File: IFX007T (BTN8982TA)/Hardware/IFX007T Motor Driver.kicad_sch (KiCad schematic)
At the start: 16 parts, among them M1 12V, SW1 ENABLE, SW2 HSS, SW3 HSS, U1 IFX007T, U2 IFX007T

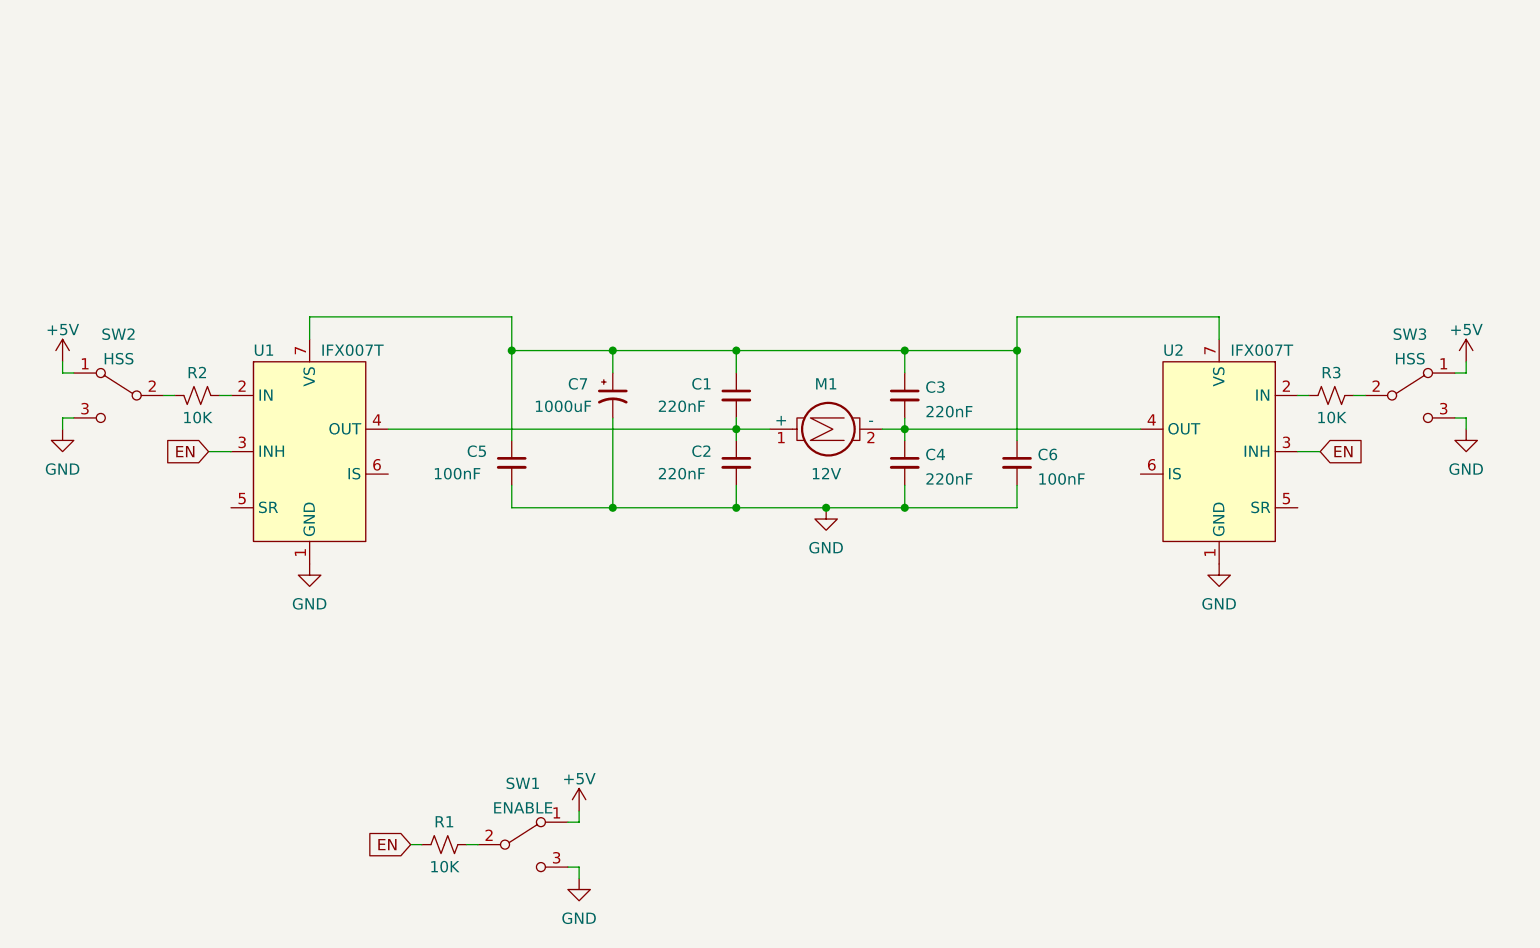
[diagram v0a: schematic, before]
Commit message: Add IS and SR circuitry
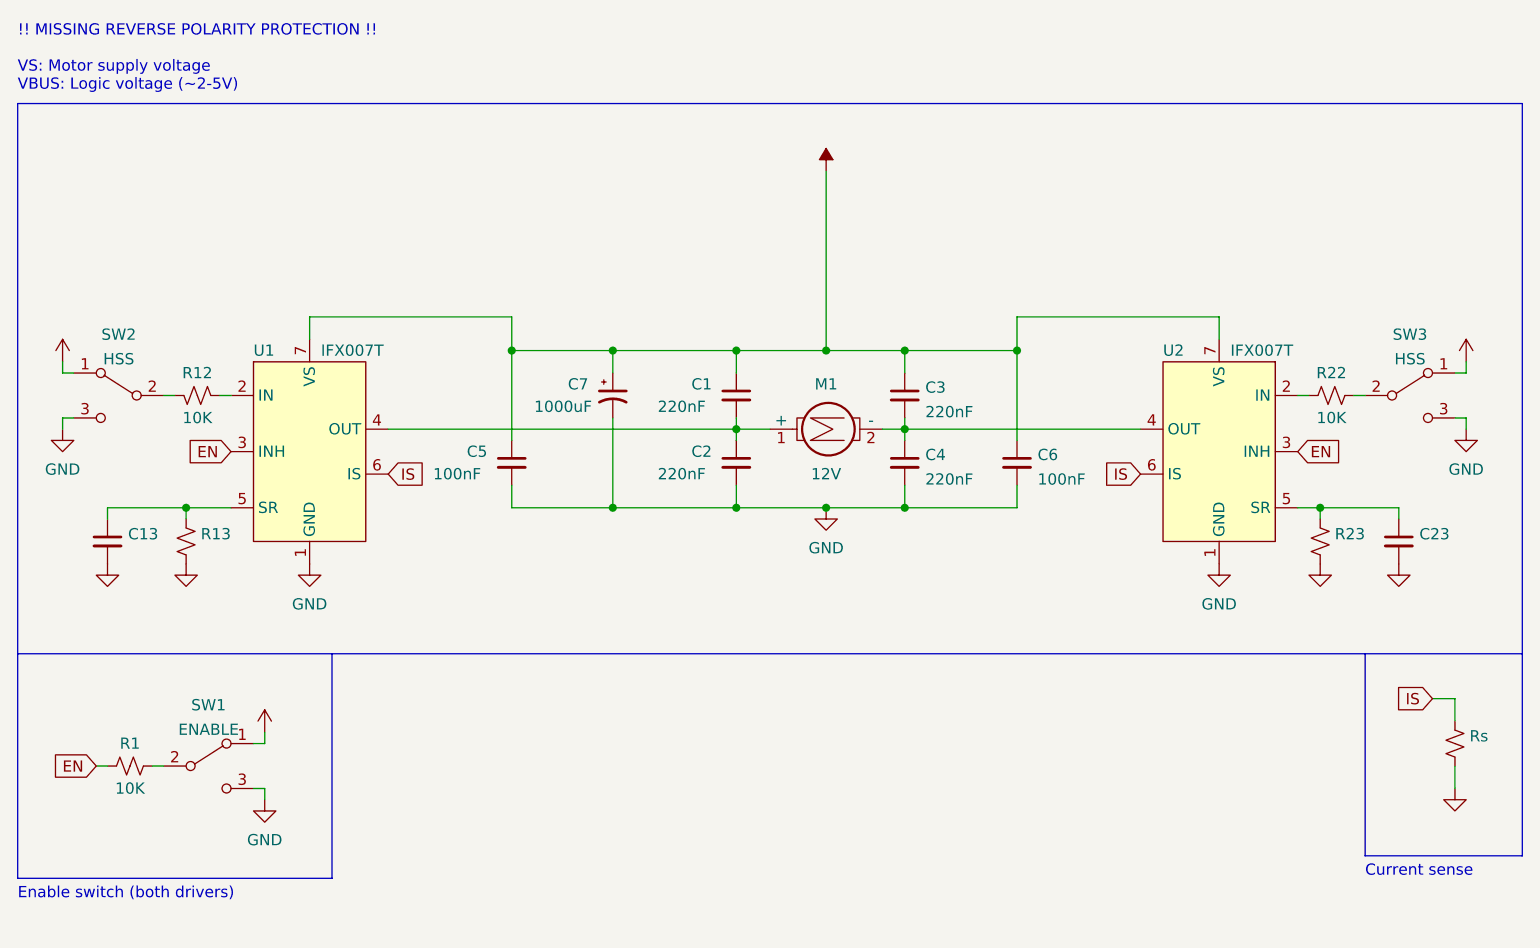
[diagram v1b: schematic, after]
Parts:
- added C13, C23: (no value), symbol Device:C_Small
- added R13, R23, Rs: (no value), symbol Device:R_Small_US
- renumbered R2 to R12, R3 to R22
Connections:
- net GND: now also C13.2, C23.2, R13.2, R23.2, Rs.2
- net VS: now reaches C1.1, C3.1, C5.1, C6.1, C7.1, U1.7 (VS), U2.7 (VS)
- net at U2.5 (SR): now also C23.1, R23.1
- net IS: now reaches U2.6 (IS)
- net IS: now also U1.6 (IS), Rs.1
- net at U1.5 (SR): now also C13.1, R13.1
- net +5V renamed VBUS
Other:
- note added: "!! MISSING REVERSE POLARITY PROTECTION !! VS: Motor supply voltage VBUS: Logic voltage (~2-5V)"
- note added: "Current sense"
- note added: "Enable switch (both drivers)"
- moved on the sheet: R1, SW1
